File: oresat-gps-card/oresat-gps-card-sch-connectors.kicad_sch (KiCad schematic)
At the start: 34 parts, among them J1 J-SAMTEC-TFM-120-01-L-D-RA, J3 J-TE-Debug-2-1734592-0

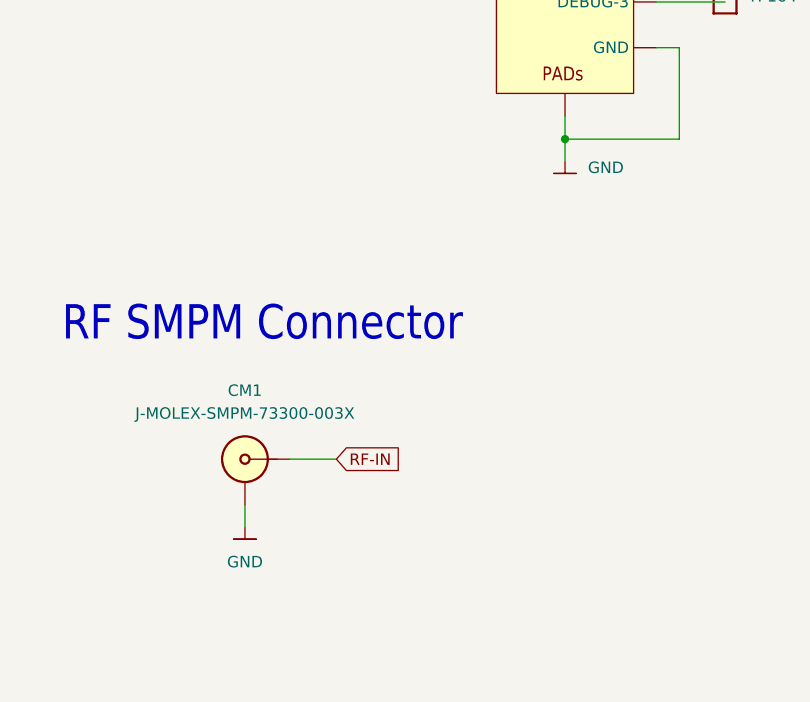
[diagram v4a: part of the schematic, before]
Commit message: Cleaned up ERC and DRC errors on GPS card
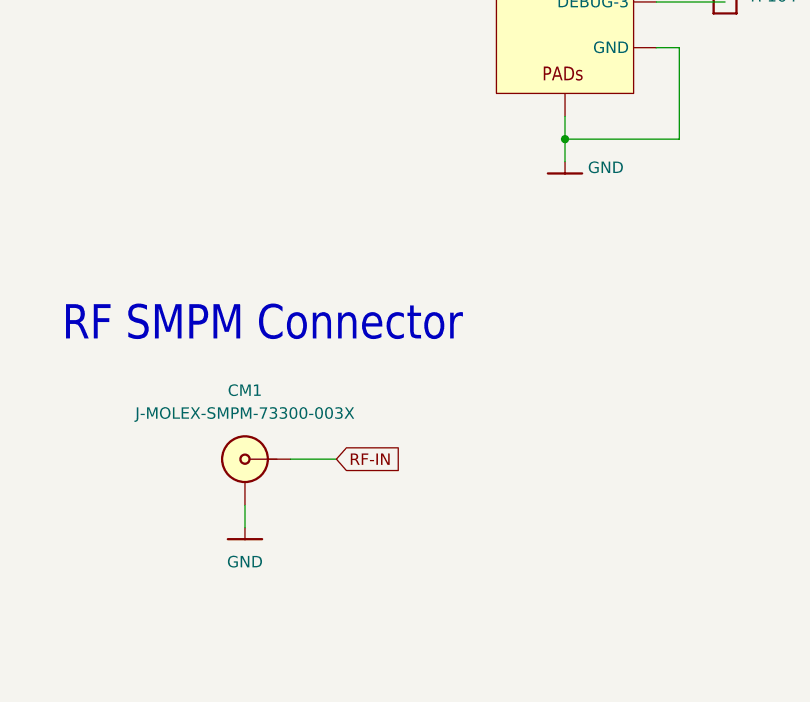
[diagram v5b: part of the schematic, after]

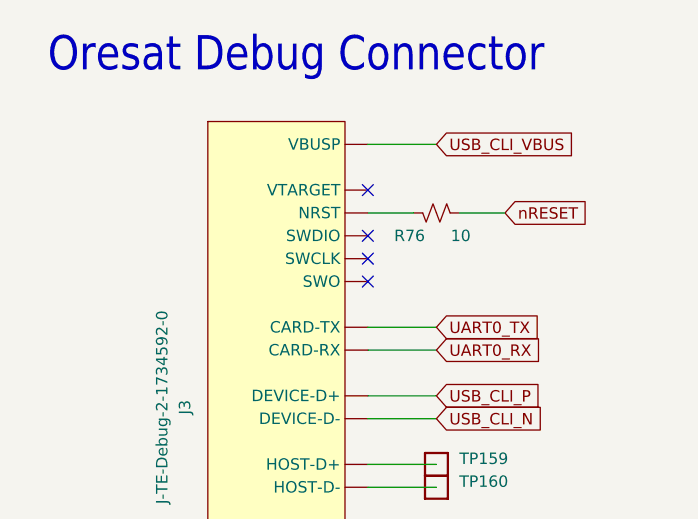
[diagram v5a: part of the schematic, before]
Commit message: Updated KiCAD 8, updated schematic sheet info, polished some schematic things, and made DNP parts DNP.
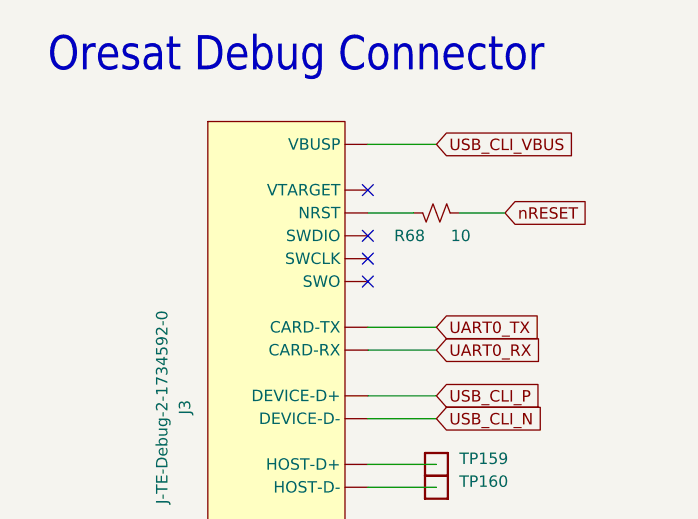
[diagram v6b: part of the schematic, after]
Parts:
- renumbered R76 to R68
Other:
- title: (none) -> OreSat GPS Card

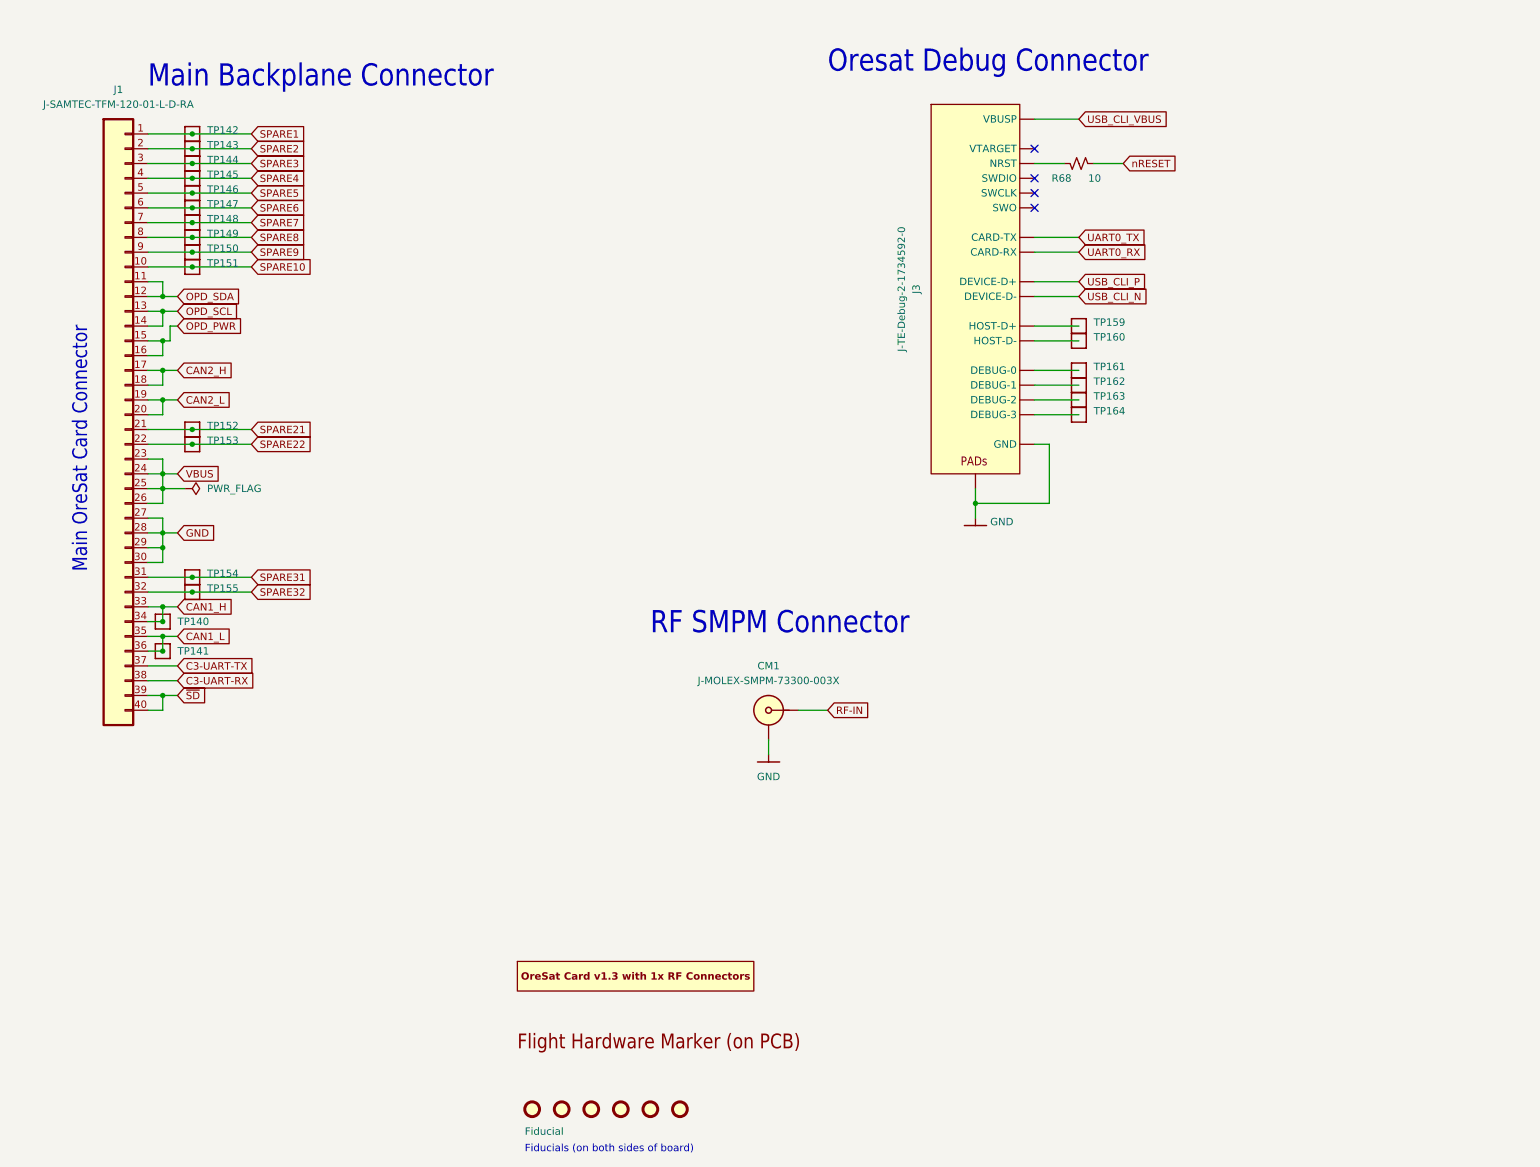
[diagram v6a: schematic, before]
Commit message: updated symbols and started new 2771 symbol
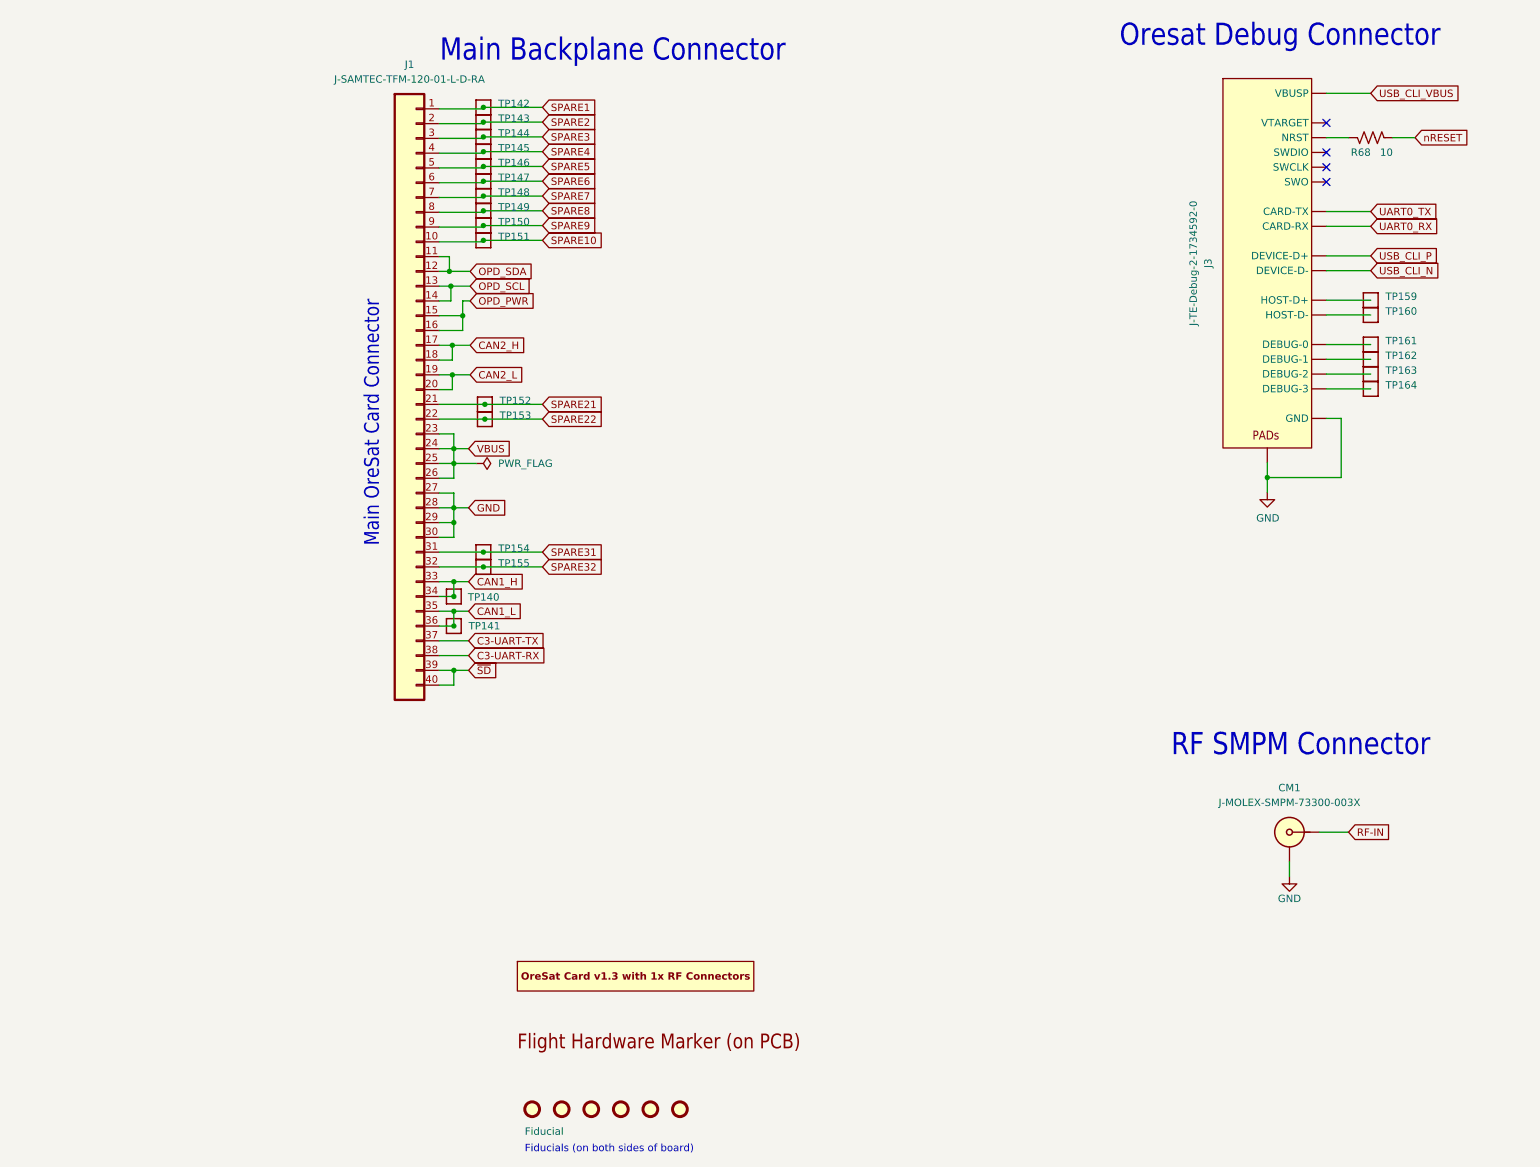
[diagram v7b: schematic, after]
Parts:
- R68: symbol Device:R_Small_US -> Device:R_US
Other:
- moved on the sheet: CM1, J1, J3, TP140, TP141, TP142, TP143, TP144, TP145, TP146, TP147, TP148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
